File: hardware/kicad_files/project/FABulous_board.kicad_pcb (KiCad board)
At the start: 4 copper layers, 101.2 x 63.5 mm, 80 parts, among them J1 Conn_01x03_Pin, J10 Conn_01x07_Pin, J11 Conn_01x03_Pin, J12 Conn_01x03_Pin, J13 Conn_01x03_Pin, J2 Conn_01x03_Pin, J3 Conn_01x03_Pin, J4 Conn_01x03_Pin, J5 Conn_01x02_Pin, J6 Conn_02x04_Odd_Even, J7 Conn_02x12_Odd_Even, J8 Conn_01x03_Pin, J9 Conn_01x05_Pin, SW1 Tactile Switch, T1 LOGO, U1 W25Q32JVSSIQ, U10 SN74LVC1G125DCKR, U11 SI5351A-B-GTR, U2 C2977809, U4 GT-USB-7010ASV, U5 FT232H, U6 AMS1117-3_3, U7 SPX1117M3-L-1-5_TR, U8 MCP1319MT-29LE-OT, U9 SN74LVC1G125DCKR, X1 TXM12M0004252DBCEO00T, X2 NX3225GA-25_000M-STD-CRG-2

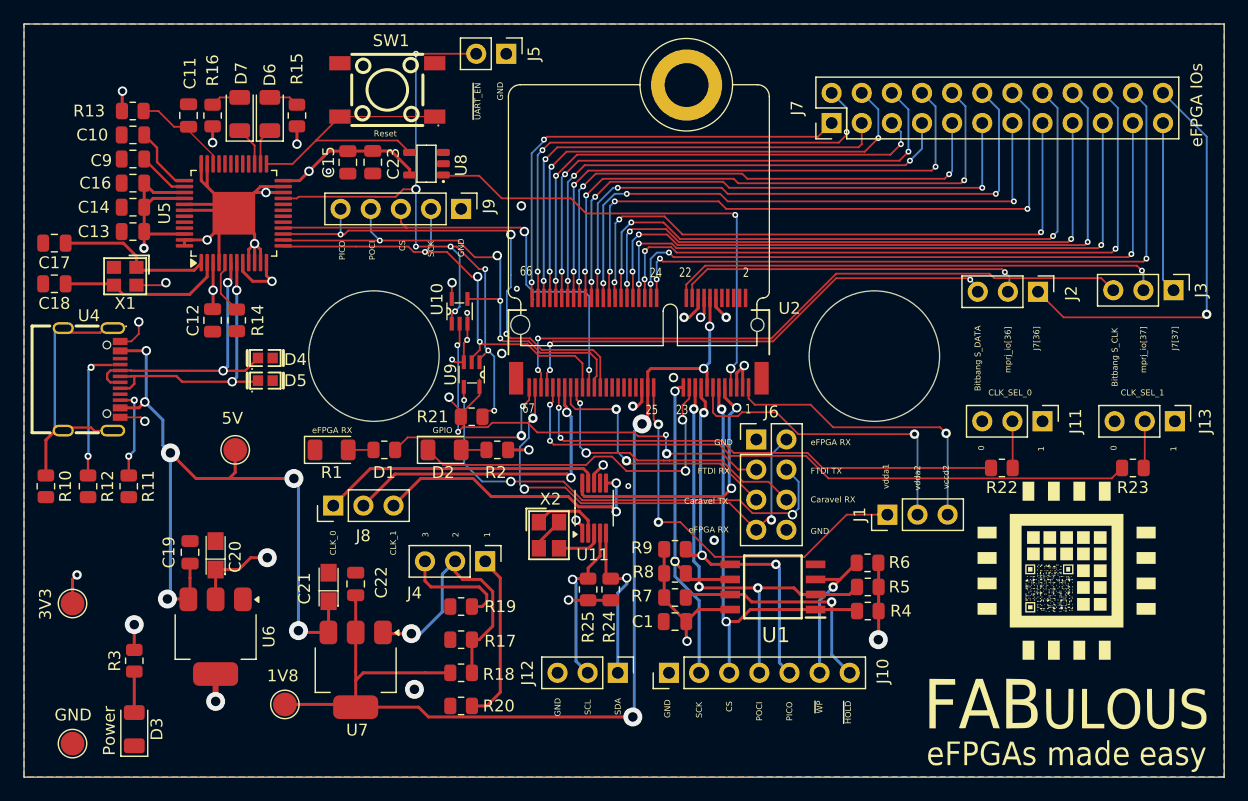
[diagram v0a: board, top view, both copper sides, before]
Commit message: fix: add offset for JLCPCB manufacturing
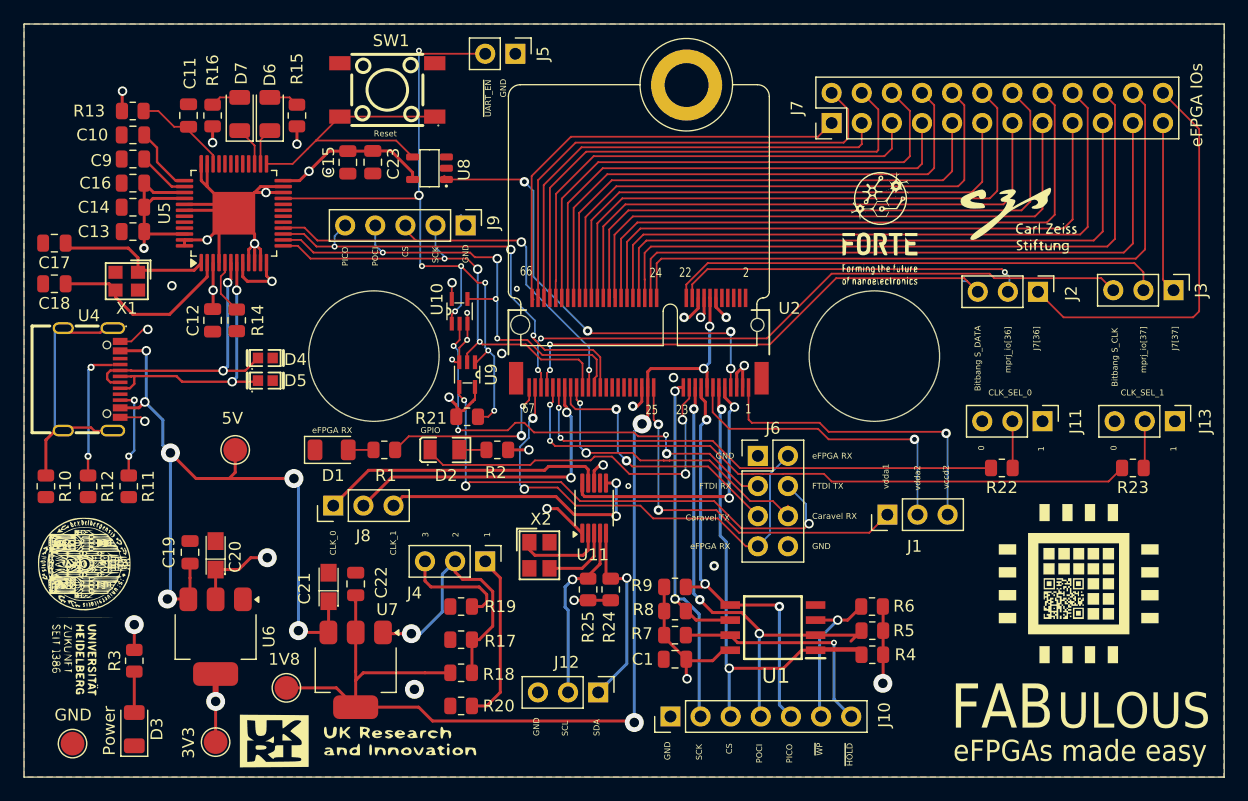
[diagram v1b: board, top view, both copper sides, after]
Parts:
- added T2: LOGO, Logos:carl_zeiss_stiftung, F.Cu at (187.5, 84.6)
- added T3: LOGO, Logos:FORTE_logo_square, F.Cu at (175.8, 85.1)
- added T4: LOGO, Logos:heidelberg-university-logo, F.Cu at (108.7, 117.1)
- added T5: LOGO, Logos:ukripluslogo, F.Cu at (131.7, 128.4)
- D2: footprint LED_SMD:LED_1206_3216Metric -> easy_eda:LED1206-RD_RED_LTST-C230CKT
- T1: footprint FABulous:fabulous_logo_qr_code_generated_30mm -> FABulous:fabulous_logo_qr_code_generated_25mm
- moved TP3 16.8 mm to (119.8, 128.5)
- moved R4 3.70 mm to (175.1, 121.2)
- moved R5 3.70 mm to (175.1, 119.1)
- moved R6 3.70 mm to (175.1, 117.1)
- moved J10 3.69 mm to (158.1, 126.4)
- moved U1 3.43 mm to (166.8, 118.9)
- moved R7 3.18 mm to (158.5, 119.5)
- moved C1 3.17 mm to (158.5, 121.5)
- moved R8 3.17 mm to (158.5, 117.5)
- moved R9 3.17 mm to (158.5, 115.4)
- moved J12 2.33 mm to (152.0, 124.3)
- moved X2 1.87 mm to (147.1, 112.8)
- moved J9 1.45 mm to (140.8, 85.0)
- moved TP4 1.40 mm to (125.7, 124.0)
- moved J6 1.39 mm to (165.5, 104.4)
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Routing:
- net /Flash_SPI.CS: track 35.9 -> 44.1 mm
- net +3V3: track 97.2 -> 105.1 mm, vias 20 -> 19
- net GND: track 70.5 -> 64.9 mm, vias 21 -> 20
- net /Flash_SPI.SCK: track 30.8 -> 35.1 mm
- net /Flash_SPI.POCI: track 38.1 -> 41.6 mm
- net /Flash_SPI.PICO: track 32.3 -> 35.7 mm
- net /FTDI_SPI.CS: track 40.3 -> 37.3 mm
- net /FTDI_UART_TX: track 40.4 -> 43.4 mm
- net /Caravel Connections/mprj_io.28: track 52.4 -> 49.6 mm, vias 3 -> 0
- net /Caravel Connections/mprj_io.29: track 55.7 -> 53.1 mm, vias 3 -> 0
- net /FTDI_SPI.PICO: track 42.2 -> 39.7 mm
- net /I2C.SDA: track 13.7 -> 16.0 mm
- net /Caravel Connections/vdda1: track 33.5 -> 31.2 mm
- net /Caravel Connections/~{RST}: track 40.8 -> 38.6 mm, vias 2 -> 4
- net Net-(U11-XB): track 3.96 -> 6.14 mm
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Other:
- board text removed: "B"
- board text removed: "ard"
- board text removed: "pen"

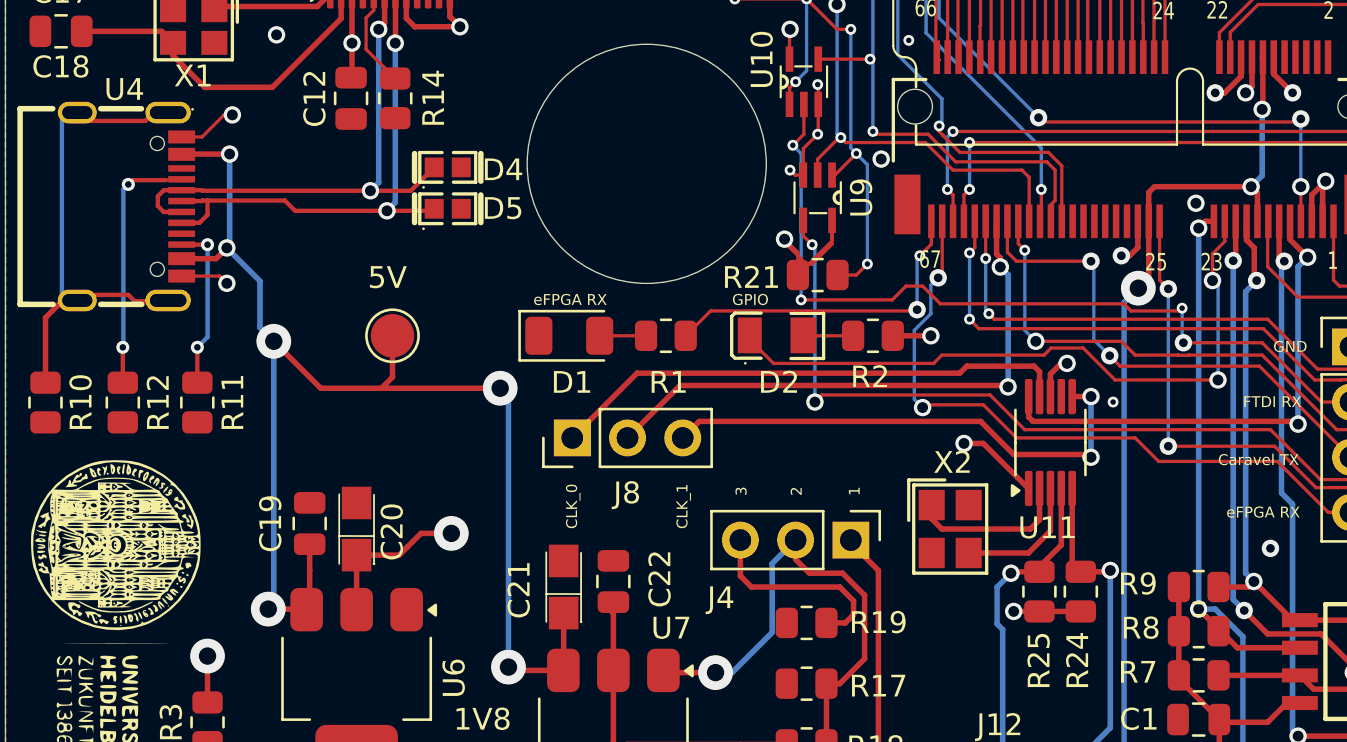
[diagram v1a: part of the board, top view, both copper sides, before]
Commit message: fix D2 LED orientation and change Pads of USB-C connector to avoid warnings, also exlude all logos from BOM
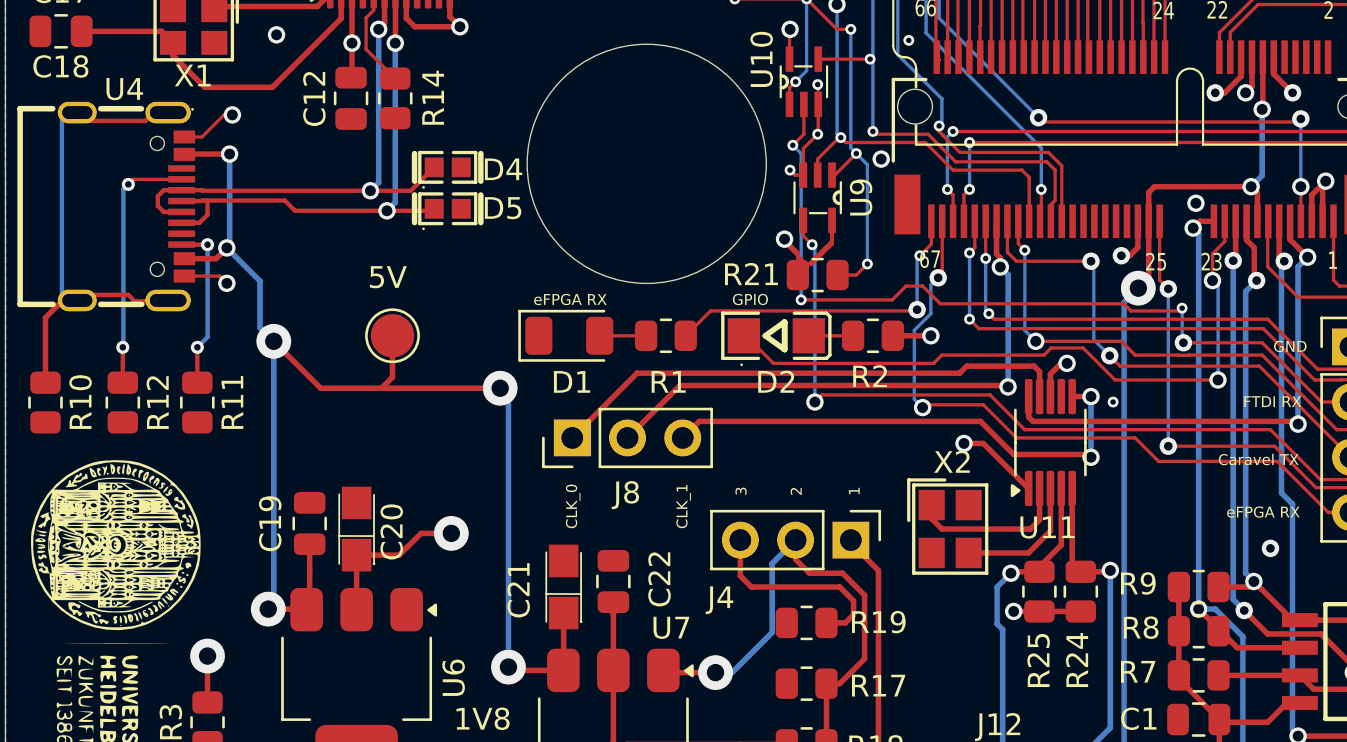
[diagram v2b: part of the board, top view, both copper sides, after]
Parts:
- D2: value C3646938 -> C965822; footprint easy_eda:LED1206-RD_RED_LTST-C230CKT -> easy_eda:LED1206-R-RD_RED
- turned D2 to 180 degrees
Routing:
- net Net-(U4-CC1): track 11.1 -> 11.8 mm

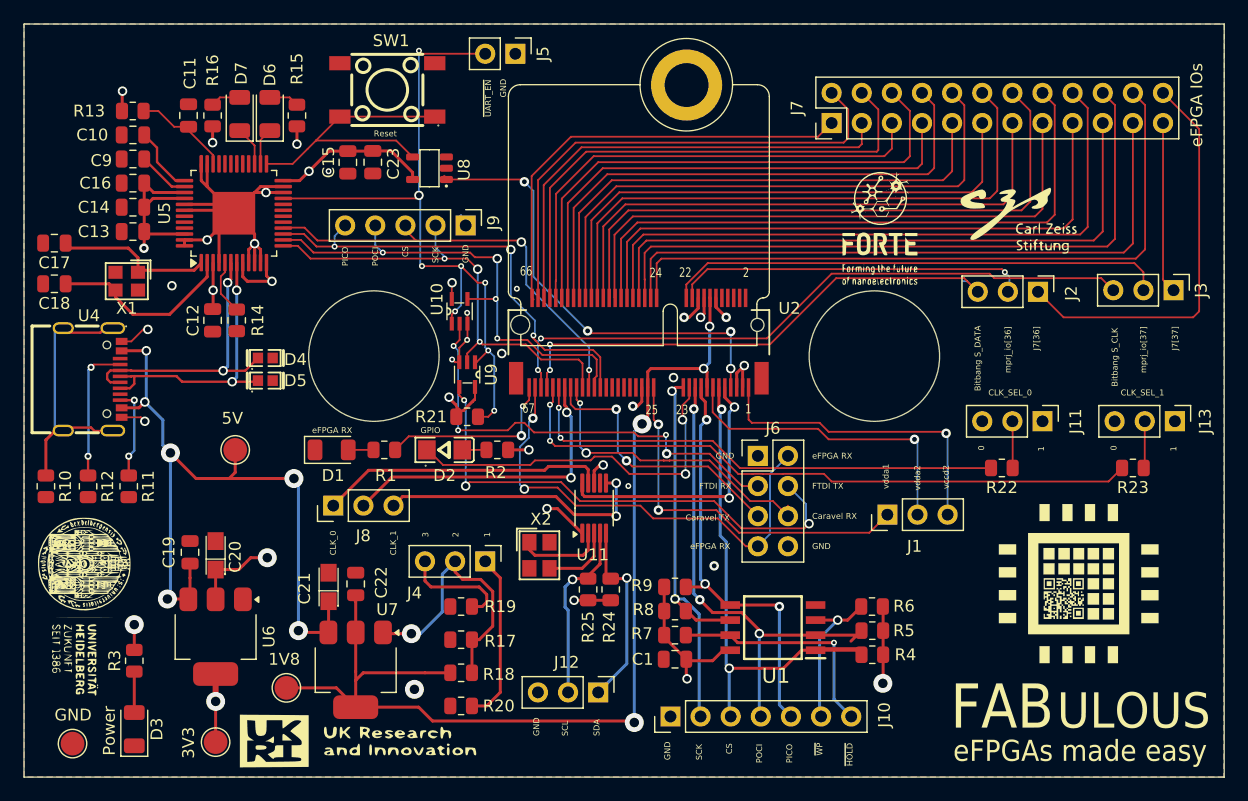
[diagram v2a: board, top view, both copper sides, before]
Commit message: fix: rename and reconnect S_DATA and S_CLK
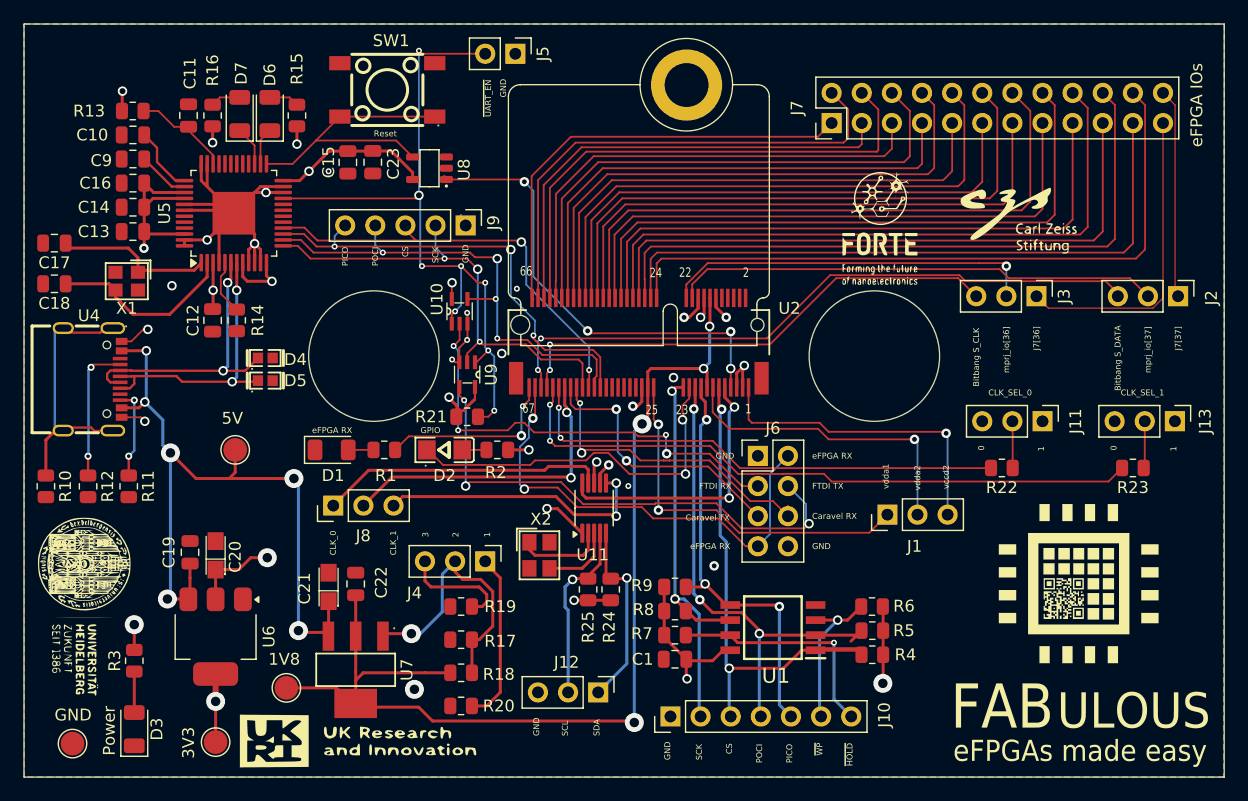
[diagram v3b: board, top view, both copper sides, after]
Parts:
- U7: value SPX1117M3-L-1-5_TR -> SPX1117M3-L_TR; footprint Package_TO_SOT_SMD:SOT-223-3_TabPin2 -> easy_eda:SOT-223-4_L6.5-W3.5-P2.30-LS7.0-BR
- moved J2 11.8 mm to (200.9, 90.9)
- moved J3 11.6 mm to (189.0, 90.9)
- turned U7 to 90 degrees
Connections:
- net /Power Conversion/ADJ renamed /Voltage Conversion/ADJ
- net /Power Conversion/ADJ_1_45 renamed /Voltage Conversion/ADJ_1_45
- net /Power Conversion/ADJ_1_6 renamed /Voltage Conversion/ADJ_1_6
- J2 pad 3: /Caravel Connections/Bitbang.S_CLK -> /Caravel Connections/Bitbang.S_DATA
- J3 pad 3: /Caravel Connections/Bitbang.S_DATA -> /Caravel Connections/Bitbang.S_CLK
- U11 pad 7: unconnected-(U11-VDDO-Pad7) -> +3V3
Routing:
- net /Caravel Connections/mprj_io.37: track 34.4 -> 17.1 mm
- net /Caravel Connections/mprj_io.36: track 14.5 -> 26.2 mm
- net /Caravel Connections/mprj_io_37_internal: track 30.0 -> 41.0 mm, vias 1 -> 0
- net /Caravel Connections/mprj_io_36_internal: track 42.3 -> 31.5 mm, vias 0 -> 1
- net +3V3: track 105.1 -> 106.9 mm, vias 19 -> 20
- net /Caravel Connections/Bitbang.S_CLK: track 44.2 -> 42.6 mm

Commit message: fix: Adjust layout to changed footprints, also optimize the routing of the USB data lines
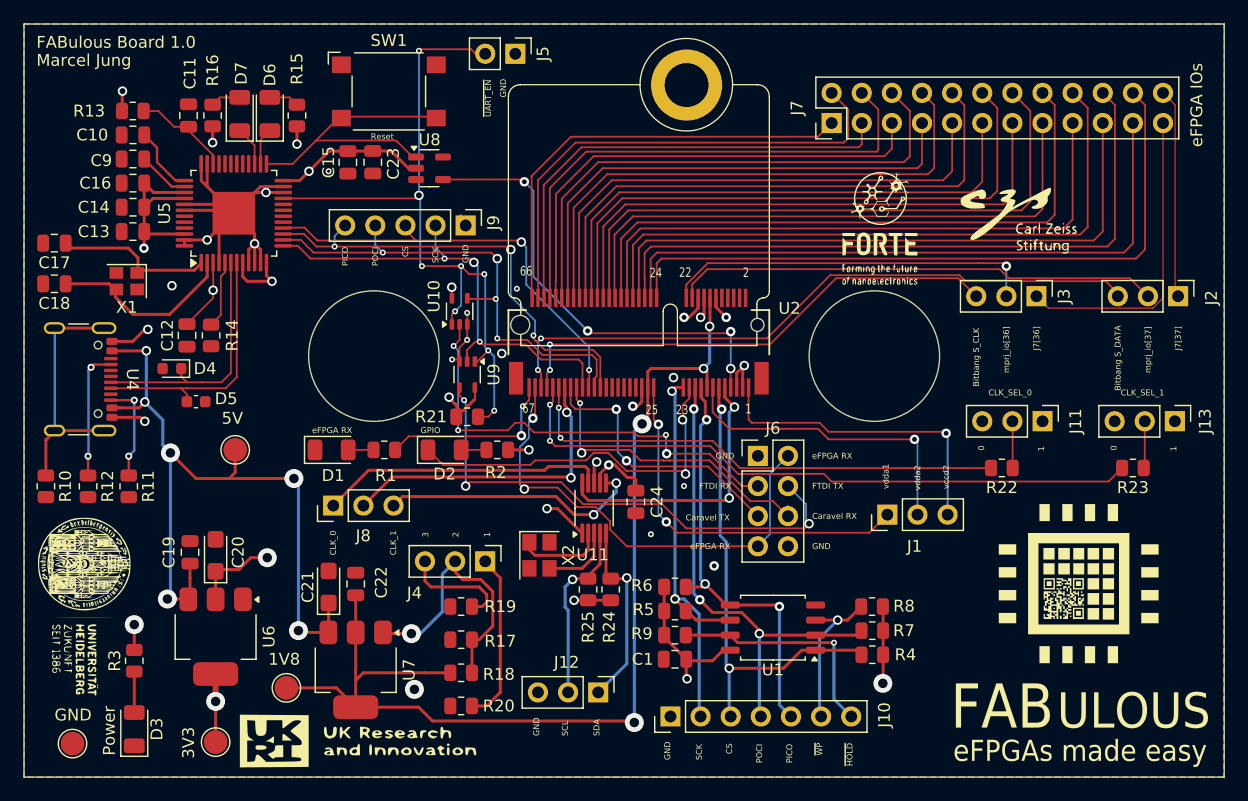
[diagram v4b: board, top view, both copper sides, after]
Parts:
- added C24: 10u, Capacitor_SMD:C_0805_2012Metric, F.Cu at (155.2, 108.3)
- C20, C21: footprint easy_eda:CASE-A_3216 -> Capacitor_Tantalum_SMD:CP_EIA-3216-10_Kemet-I
- D2: footprint easy_eda:LED1206-R-RD_RED -> LED_SMD:LED_1206_3216Metric
- D4: footprint easy_eda:D0603-BI -> Diode_SMD:D_0603_1608Metric
- D5: footprint easy_eda:D0603-BI -> Capacitor_SMD:C_0603_1608Metric
- H1: value MICROMOD-Standoff -> M.2 Standoff
- SW1: footprint easy_eda:SW_SMD_4P_L6.0_W6.0-P4.5-LS8.6 -> Button_Switch_SMD:SW_SPST_Omron_B3FS-101xP
- T1: footprint FABulous:fabulous_logo_qr_code_generated_25mm -> Logos:fabulous_logo_qr_code_generated_25mm
- U1: footprint strive_foot_prints:SOIC127P790X216-8N -> Package_SO:SOIC-8_5.23x5.23mm_P1.27mm
- U10, U9: footprint strive_foot_prints:SOT65P210X110-5N -> Package_TO_SOT_SMD:Texas_R-PDSO-G5_DCK-5
- U4: footprint easy_eda:USB-C-SMD_G-SWITCH_GT-USB-7010ASV -> Customized:USB_C_Receptacle_GCT_USB4105-xx-A_16P_TopMnt_Horizontal
- U7: footprint easy_eda:SOT-223-4_L6.5-W3.5-P2.30-LS7.0-BR -> Package_TO_SOT_SMD:SOT-223-3_TabPin2
- U8: footprint Caravel_Board:PoR_5_SOT23 -> Package_TO_SOT_SMD:SOT-23-5
- X1: footprint easy_eda:CRYSTAL-SMD_4P-L2.5-W2.0-BL -> Crystal:Crystal_SMD_2520-4Pin_2.5x2.0mm
- X2: footprint easy_eda:CRYSTAL-SMD_4P-L3.2-W2.5-BL -> Crystal:Crystal_SMD_3225-4Pin_3.2x2.5mm
- moved D4 7.92 mm to (116.1, 97.0), turned to 180 degrees
- moved D5 6.11 mm to (118.1, 99.8)
- moved C12 2.50 mm to (117.3, 94.2)
- moved R14 2.50 mm to (119.4, 94.2)
- moved U4 2.07 mm to (107.2, 97.9)
- moved SW1 0.18 mm to (134.4, 73.7), turned to 0 degrees
- turned D2 to 0 degrees
- turned U7 to -90 degrees
- turned U8 to 0 degrees
- renumbered R8 to R5, R9 to R6, R5 to R7, R6 to R8, R7 to R9
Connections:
- SW1 pad 1: /PC Connection/~{MR} -> GND
- SW1 pad 2: GND -> /PC Connection/~{MR}
- U4 pad A6: /PC Connection/D+ -> unconnected-(U4-D+-PadA6)
- U4 pad B7: /PC Connection/D- -> unconnected-(U4-D--PadB7)
- U8 pad 1: /Caravel Connections/~{RST} -> /PC Connection/~{MR}
- U8 pad 2: GND -> +3V3
- U8 pad 4: /PC Connection/~{MR} -> /Caravel Connections/~{RST}
- U8 pad 5: +3V3 -> GND
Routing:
- net +3V3: track 106.9 -> 112.4 mm
- net /Flash_SPI.CS: track 44.1 -> 40.4 mm
- net /PC Connection/D-: track 25.2 -> 21.5 mm, vias 2 -> 0
- net /PC Connection/D+: track 24.1 -> 22.0 mm, vias 2 -> 0
- net +5V: track 63.7 -> 65.2 mm
- net /CLK_efpga_1: track 23.4 -> 22.1 mm
- net /Flash_SPI.POCI: track 41.6 -> 40.4 mm
- net GND: track 64.7 -> 65.9 mm, vias 20 -> 21
- net /PC Connection/REF: track 4.66 -> 5.71 mm
- net /FTDI_SPI.SCK: track 40.2 -> 41.0 mm
- net Net-(U4-CC2): track 7.92 -> 8.70 mm
- net Net-(U4-CC1): track 11.8 -> 11.0 mm
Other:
- board text added: "FABulous Board 1.0"
- board text added: "Marcel Jung"
